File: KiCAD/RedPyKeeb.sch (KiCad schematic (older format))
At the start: 11 parts, among them J0 Conn_01x04, J1 Conn_01x04, U0 USB_Pico, U1 MCP23017-E/SO, U10 PCA9306DP, U11 TXB0104D, U2 MCP23017-E/SO, U3 MCP23017-E/SO

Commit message: Update KiCAD files.
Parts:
- added C4, C5, C7: 0805B101K100CT, Capacitor_SMD:C_0805_2012Metric_Pad1.18x1.45mm_HandSolder, symbol Device:C
- added J2: Conn_01x04, Connector_JST:JST_EH_S4B-EH_1x04_P2.50mm_Horizontal, symbol Connector_Generic:Conn_01x04
- added R1, R2, R4, R5: APC0805B1K00N, Resistors_SMD:R_0805_HandSoldering, symbol Device:R_Small_US
- added R3: ERJ-6RED2003V, Resistors_SMD:R_0805_HandSoldering, symbol Device:R_Small_US
- C1, C2, C3: symbol Device:CP -> Device:C; Mouser No (none) -> 791-0805B104K100CT
- J0, J1: Mouser No (none) -> 485-3955
- U0: value USB_Pico -> ~
- U1, U2, U3: Mouser No (none) -> 579-MCP23017-E/SO
- U10: footprint Package_SO:SO-8_3.9x4.9mm_P1.27mm -> Package_SO:SSOP-8_2.95x2.8mm_P0.65mm; Mouser No (none) -> PCA9306DP,118
- U11: Mouser No (none) -> TXB0104D
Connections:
- net GNDPWR: now also C4.1, C5.1, C7.1
- net I2C_SCL0: now also R2.2
- net I2C_SDA0: now also R1.2
- net MAIN_VBUS: now also C5.2, R1.1, R2.1, R3.1; no longer U10.7 (VREF2), U10.8 (EN)
- net PICO_33_REF: now also C7.2, R4.2, R5.2
- net PICO_SCL0: now also R5.1
- net PICO_SDA0: now also R4.1
- net at U0.21 (GPIO16): now also J2.4 (Pin_4)
- net at U0.22 (GPIO17): now also J2.3 (Pin_3)
- net at U0.24 (GPIO18): now also J2.2 (Pin_2)
- net at U0.25 (GPIO19): now also J2.1 (Pin_1)
- new net: C4.2, R3.2, U10.7 (VREF2), U10.8 (EN)
- no-connect marks 40 -> 36
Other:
- moved on the sheet: U0, U10, U11

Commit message: Update firmware and KiCAD files.
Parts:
- J2: footprint Connector_JST:JST_EH_S4B-EH_1x04_P2.50mm_Horizontal -> Connector_JST:JST_EH_S7B-EH_1x07_P2.50mm_Horizontal; symbol Connector_Generic:Conn_01x04 -> Connector_Generic:Conn_01x07
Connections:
- net at J2.1 (Pin_1): now also U0.36 (3V3); no longer U0.25 (GPIO19)
- net at J2.2 (Pin_2): now also U0.38 (GND); no longer U0.24 (GPIO18)
- net at J2.3 (Pin_3): now also U0.24 (GPIO18); no longer U0.22 (GPIO17)
- net at J2.4 (Pin_4): now also U0.25 (GPIO19); no longer U0.21 (GPIO16)
- net at U0.26 (GPIO20): now also J2.6 (Pin_6)
- net at U0.27 (GPIO21): now also J2.7 (Pin_7)
- new net: J2.5 (Pin_5), U0.22 (GPIO17)
- no-connect marks 36 -> 33
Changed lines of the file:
@@
 MAIN_VBUS
 NoConn ~ 3350 2350
-NoConn ~ 4750 2550
 NoConn ~ 4750 2650
 NoConn ~ 4750 2750
@@
 NoConn ~ 4750 3250
 NoConn ~ 4750 3350
-NoConn ~ 4750 3450
-NoConn ~ 4750 3550
 NoConn ~ 4750 3850
 NoConn ~ 3350 4050
@@
 Wire Wire Line
 	1650 4750 3900 4750
-NoConn ~ 4750 2350
 Text Notes 2650 1200 0    39   ~ 0
 0805B104K100CT for capacitors\n100nF
@@
 	1400 2800 1600 2800
 $Comp
-L Connector_Generic:Conn_01x04 J2
+L Connector_Generic:Conn_01x07 J2
 U 1 1 60E13064
-P 5200 3750
-F 0 "J2" H 5118 3325 50  0000 C CNN
-F 1 "Conn_01x04" H 5118 3416 50  0000 C CNN
-F 2 "Connector_JST:JST_EH_S4B-EH_1x04_P2.50mm_Horizontal" H 5200 3750 50  0001 C CNN
-F 3 "" H 5200 3750 50  0001 C CNN
-F 4 "485-3955" H 5200 3750 50  0001 C CNN "Mouser No"
-	1    5200 3750
+P 5350 3650
+F 0 "J2" H 5268 3225 50  0000 C CNN
+F 1 "Conn_01x04" H 5268 3316 50  0000 C CNN
+F 2 "Connector_JST:JST_EH_S7B-EH_1x07_P2.50mm_Horizontal" H 5350 3650 50  0001 C CNN
+F 3 "" H 5350 3650 50  0001 C CNN
+F 4 "485-3955" H 5350 3650 50  0001 C CNN "Mouser No"
+	1    5350 3650
 	1    0    0    -1
 $EndComp
 Wire Wire Line
-	5000 3650 4750 3650
-Wire Wire Line
-	4750 3750 5000 3750
-Wire Wire Line
-	5000 3850 4850 3850
-Wire Wire Line
-	4850 3850 4850 3950
-Wire Wire Line
-	4850 3950 4750 3950
-Wire Wire Line
-	5000 3950 4900 3950
-Wire Wire Line
-	4900 3950 4900 4050
-Wire Wire Line
-	4900 4050 4750 4050
+	4750 2350 4900 2350
+Wire Wire Line
+	4900 2350 4900 3450
+Wire Wire Line
+	5000 3350 5000 2550
+Wire Wire Line
+	5000 2550 4750 2550
+Wire Wire Line
+	5000 3350 5150 3350
+Wire Wire Line
+	4900 3450 5150 3450
+Wire Wire Line
+	5100 3750 5100 3550
+Wire Wire Line
+	5100 3550 5150 3550
+Wire Wire Line
+	4750 3650 5150 3650
+Wire Wire Line
+	4750 3750 5100 3750
+Wire Wire Line
+	5150 3750 5150 3800
+Wire Wire Line
+	5150 3800 4800 3800
+Wire Wire Line
+	4800 3800 4800 3950
+Wire Wire Line
+	4800 3950 4750 3950
+Wire Wire Line
+	4750 3550 4950 3550
+Wire Wire Line
+	4950 3550 4950 3850
+Wire Wire Line
+	4950 3850 5150 3850
+Wire Wire Line
+	4750 3450 4850 3450
+Wire Wire Line
+	4850 3450 4850 3950
+Wire Wire Line
+	4850 3950 5150 3950
+NoConn ~ 4750 4050
 $EndSCHEMATC

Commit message: Update KiCAD files.
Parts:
- U10: value PCA9306DP -> PCA9306DP,118; footprint Package_SO:SSOP-8_2.95x2.8mm_P0.65mm -> Package_SO:TSSOP-8_3x3mm_P0.65mm; Mouser No PCA9306DP,118 -> 771-PCA9306DP-T
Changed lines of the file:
@@
 P 2100 1950
 F 0 "U10" H 2100 1269 50  0000 C CNN
-F 1 "PCA9306DP" H 2100 1360 50  0000 C CNN
-F 2 "Package_SO:SSOP-8_2.95x2.8mm_P0.65mm" H 2100 1500 50  0001 C CNN
+F 1 "PCA9306DP,118" H 2100 1360 50  0000 C CNN
+F 2 "Package_SO:TSSOP-8_3x3mm_P0.65mm" H 2100 1500 50  0001 C CNN
 F 3 "https://www.nxp.com/docs/en/data-sheet/PCA9306.pdf" H 1800 2400 50  0001 C CNN
-F 4 "PCA9306DP,118" H 2100 1950 50  0001 C CNN "Mouser No"
+F 4 "771-PCA9306DP-T" H 2100 1950 50  0001 C CNN "Mouser No"
 	1    2100 1950
 	-1   0    0    1

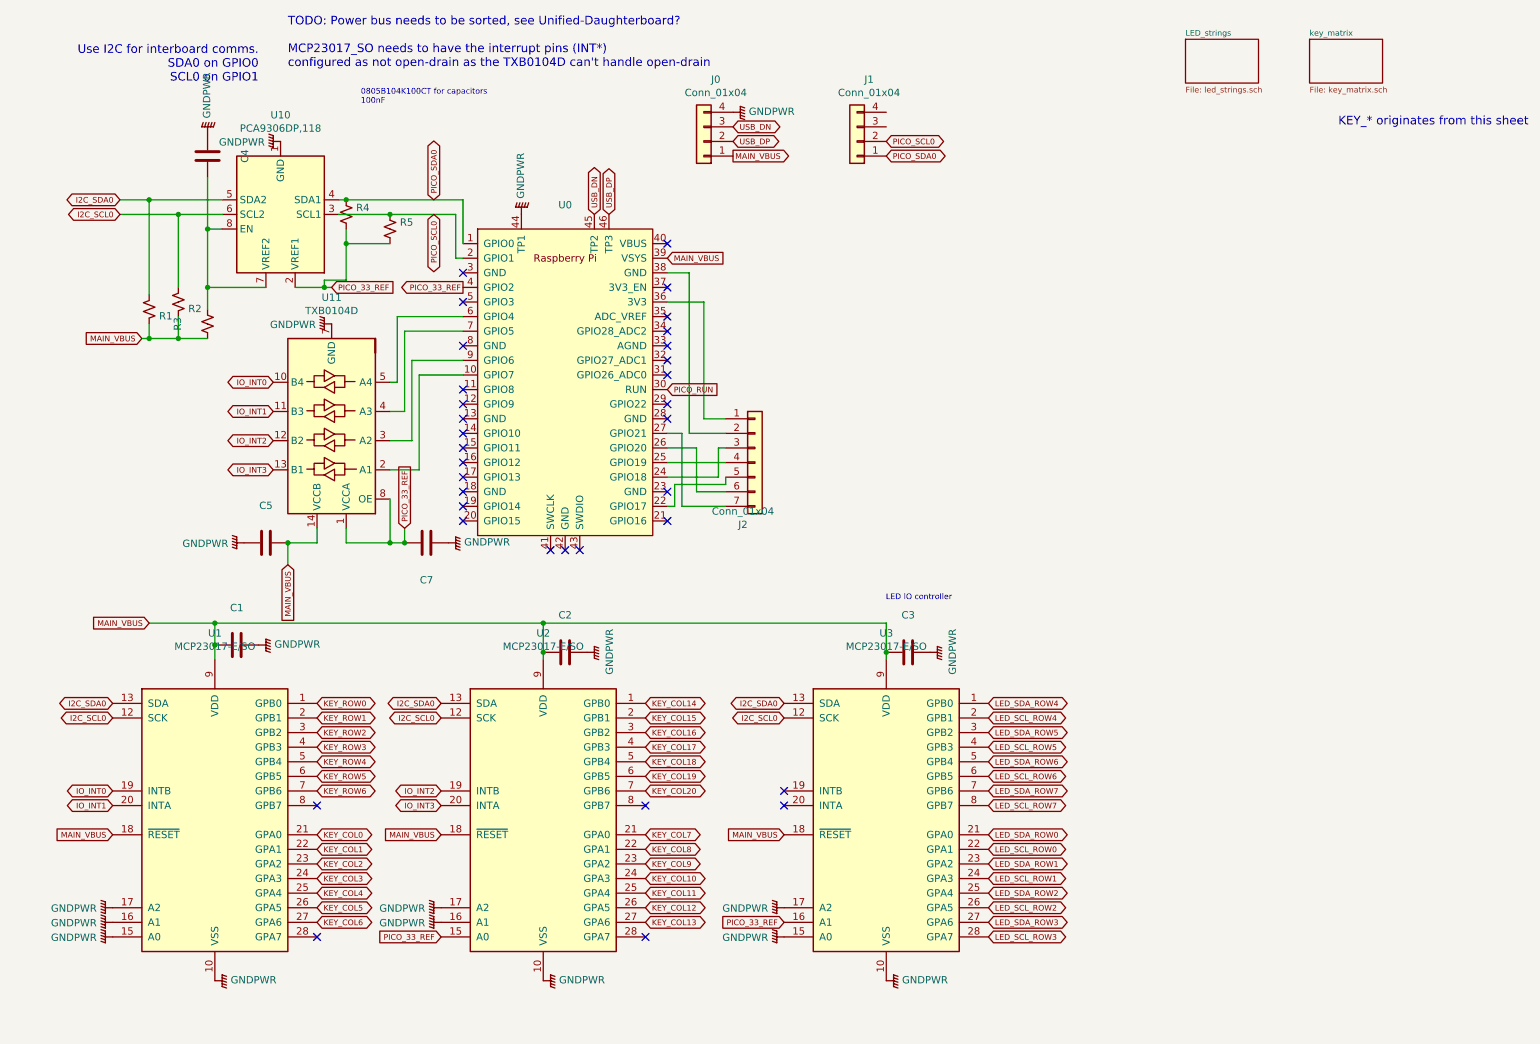
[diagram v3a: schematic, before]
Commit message: KiCAD and firmware updates, first working firmware and half way through a board rewire after the initial semi-working board. Firmware has no real LED control other than the power budget system and pin setup. Although the firmware works, it is not a working keyboard, yet.
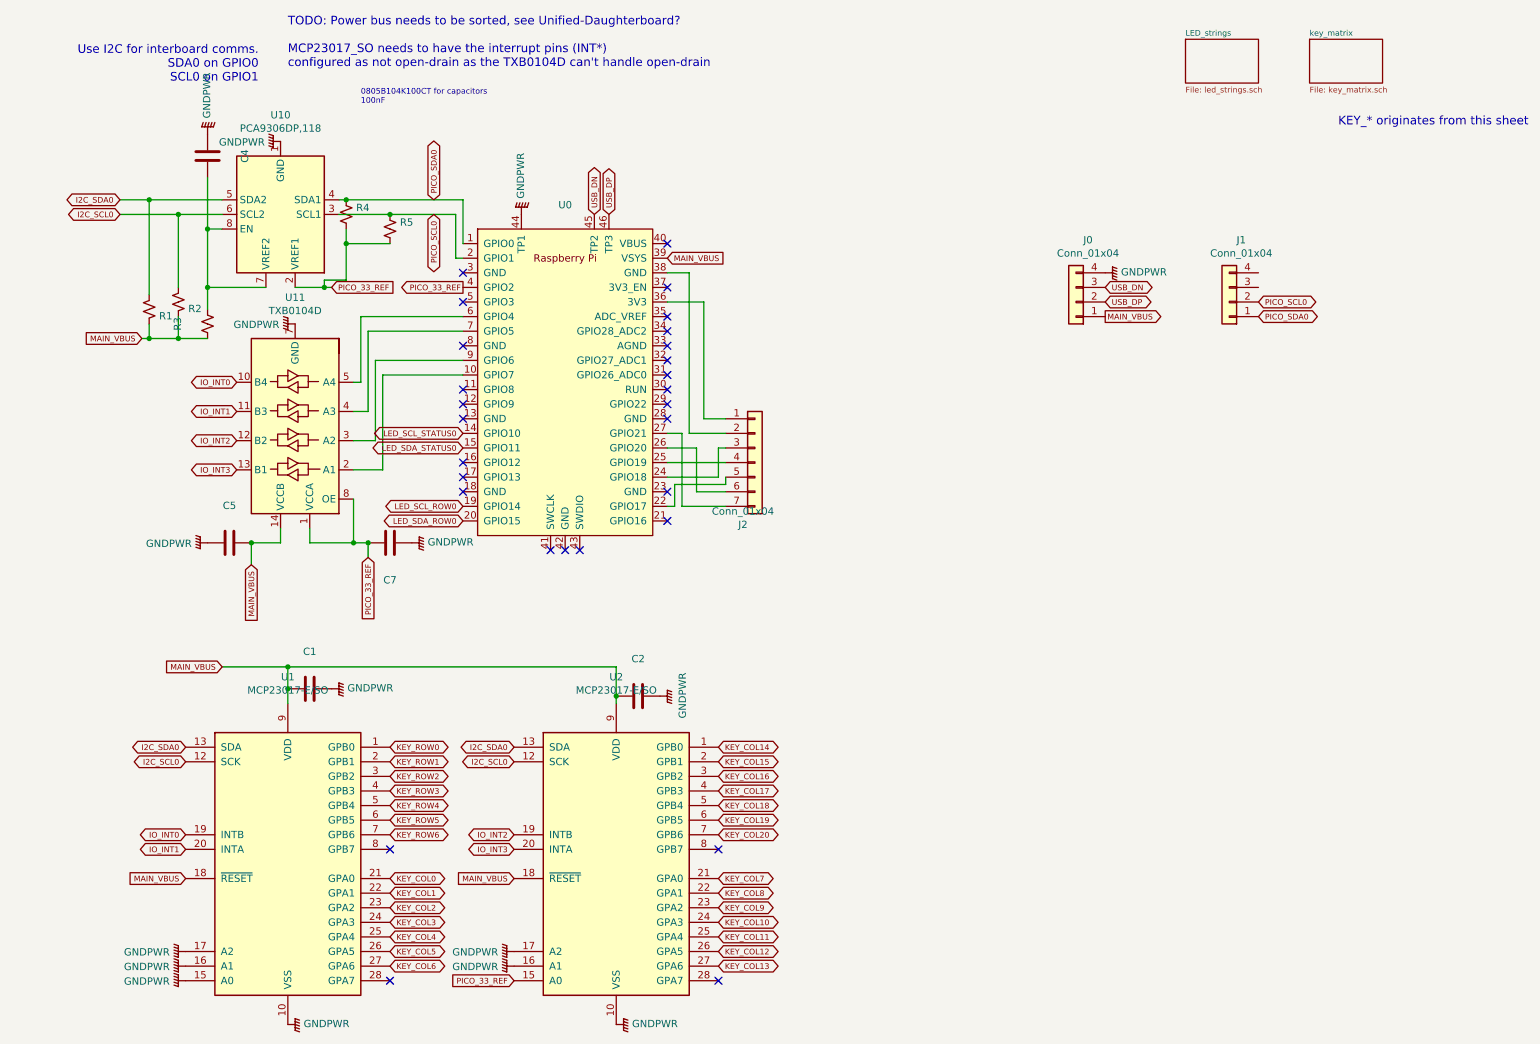
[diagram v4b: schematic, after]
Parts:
- removed C3: 0805B104K100CT, Capacitors_SMD:C_0805_HandSoldering, symbol Device:C
- removed U3: MCP23017-E/SO, Package_SO:SOIC-28W_7.5x17.9mm_P1.27mm, symbol Interface_Expansion:MCP23017_SO
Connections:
- net LED_SCL_ROW0: now also U0.19 (GPIO14)
- net LED_SDA_ROW0: now also U0.20 (GPIO15)
- net LED_SCL_STATUS0: now reaches U0.14 (GPIO10)
- net LED_SDA_STATUS0: now reaches U0.15 (GPIO11)
- net PICO_RUN: no longer names the net of U0.30 (RUN)
- no-connect marks 33 -> 28
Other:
- note removed: "LED IO controller"
- moved on the sheet: C1, C2, C5, C7, J0, J1, U1, U11, U2
